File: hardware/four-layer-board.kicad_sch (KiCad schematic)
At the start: 16 parts, among them Q1 AO3401A, U2 AMS1117-3.3

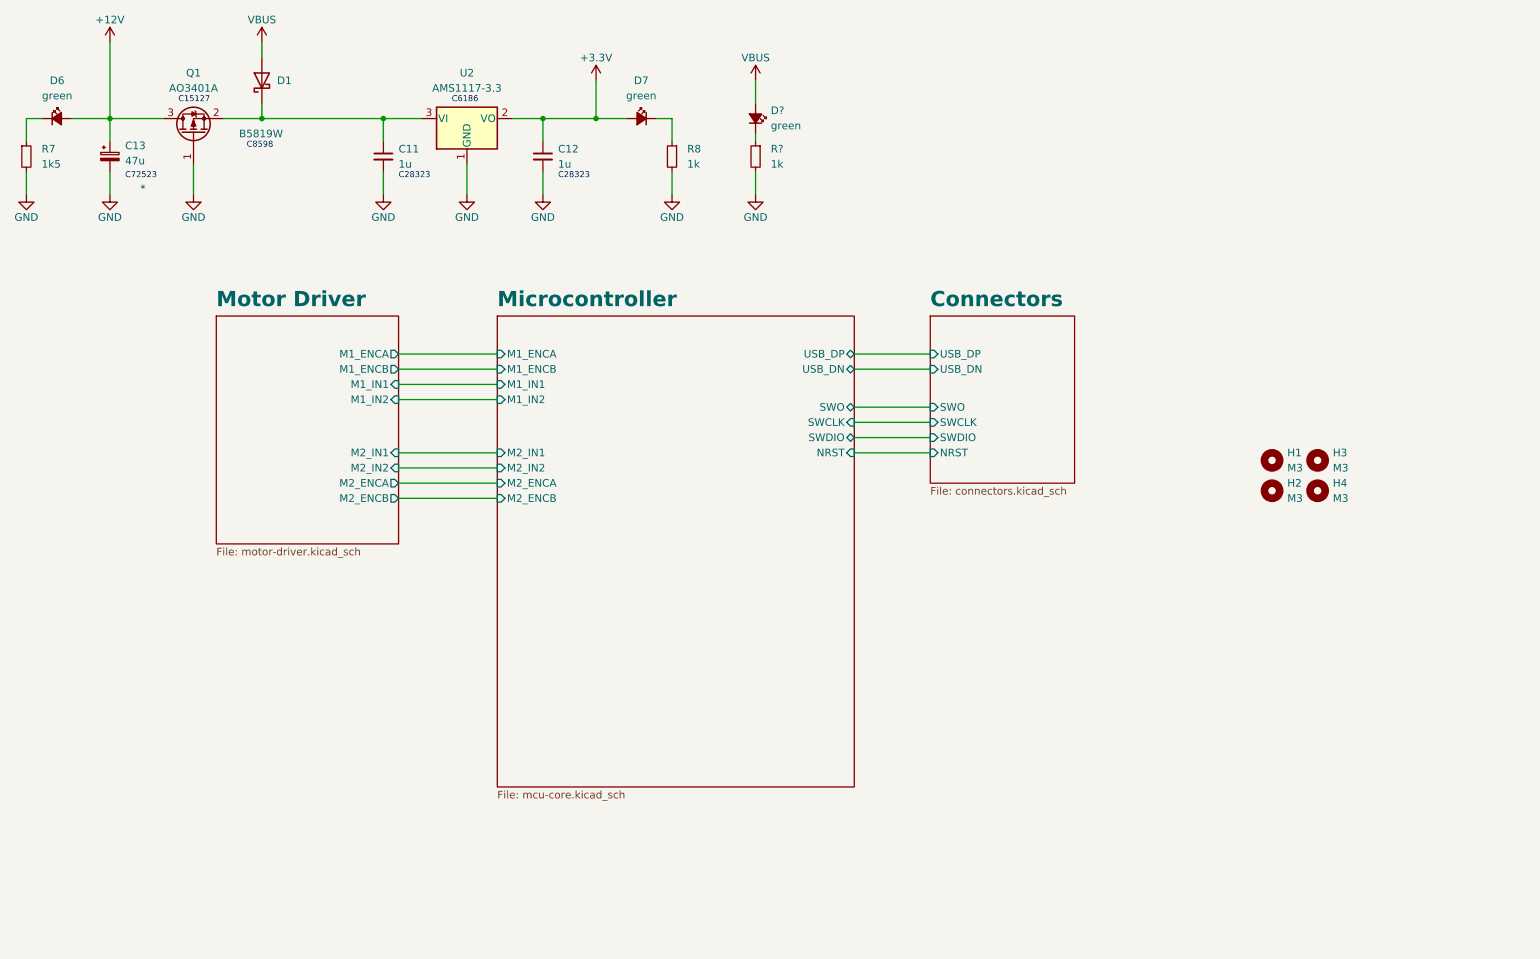
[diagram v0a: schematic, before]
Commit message: Moved hardware to separate directory
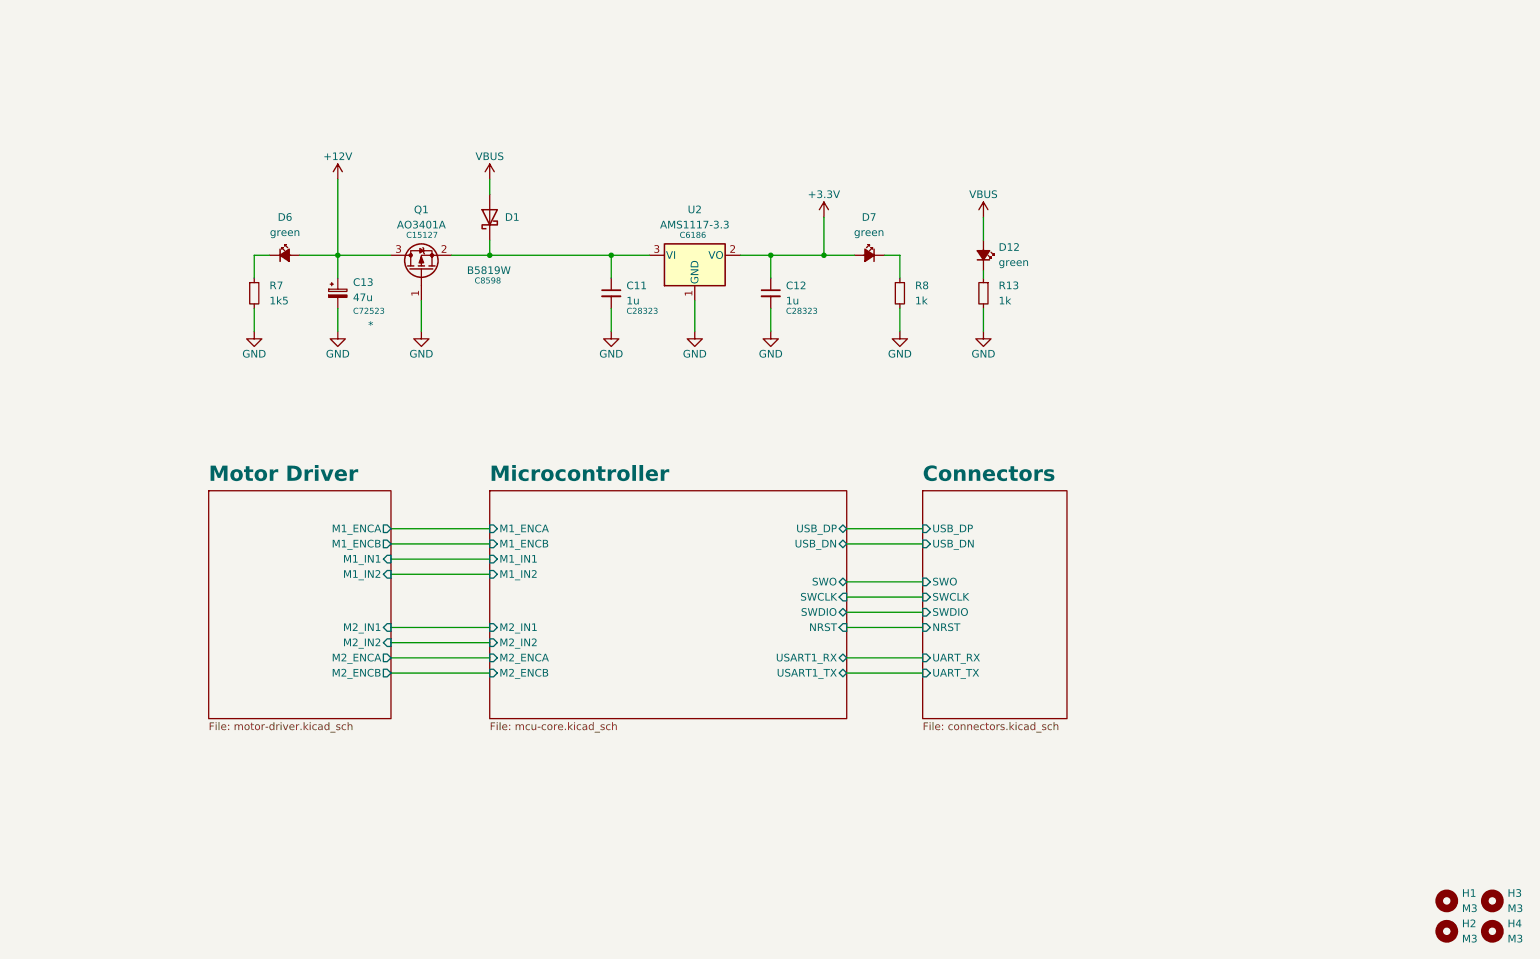
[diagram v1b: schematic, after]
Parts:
- gave numbers to parts that had none: 2
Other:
- sheet Connectors ports: added UART_RX, UART_TX; removed none
- sheet Microcontroller ports: added USART1_RX, USART1_TX; removed none
- company: (none) -> Sampreet SARKAR
- moved on the sheet: C11, C12, C13, D1, D12, D6, D7, H1, H2, H3, H4, Q1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

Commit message: Added pin assignments in firmware
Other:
- title: (none) -> Posit: A STM32 based DC motor controller
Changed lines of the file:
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@@
   (paper "A4")
   (title_block
+    (title "Posit: A STM32 based DC motor controller")
+    (date "2023-06-25")
     (rev "A")
     (company "Sampreet SARKAR")

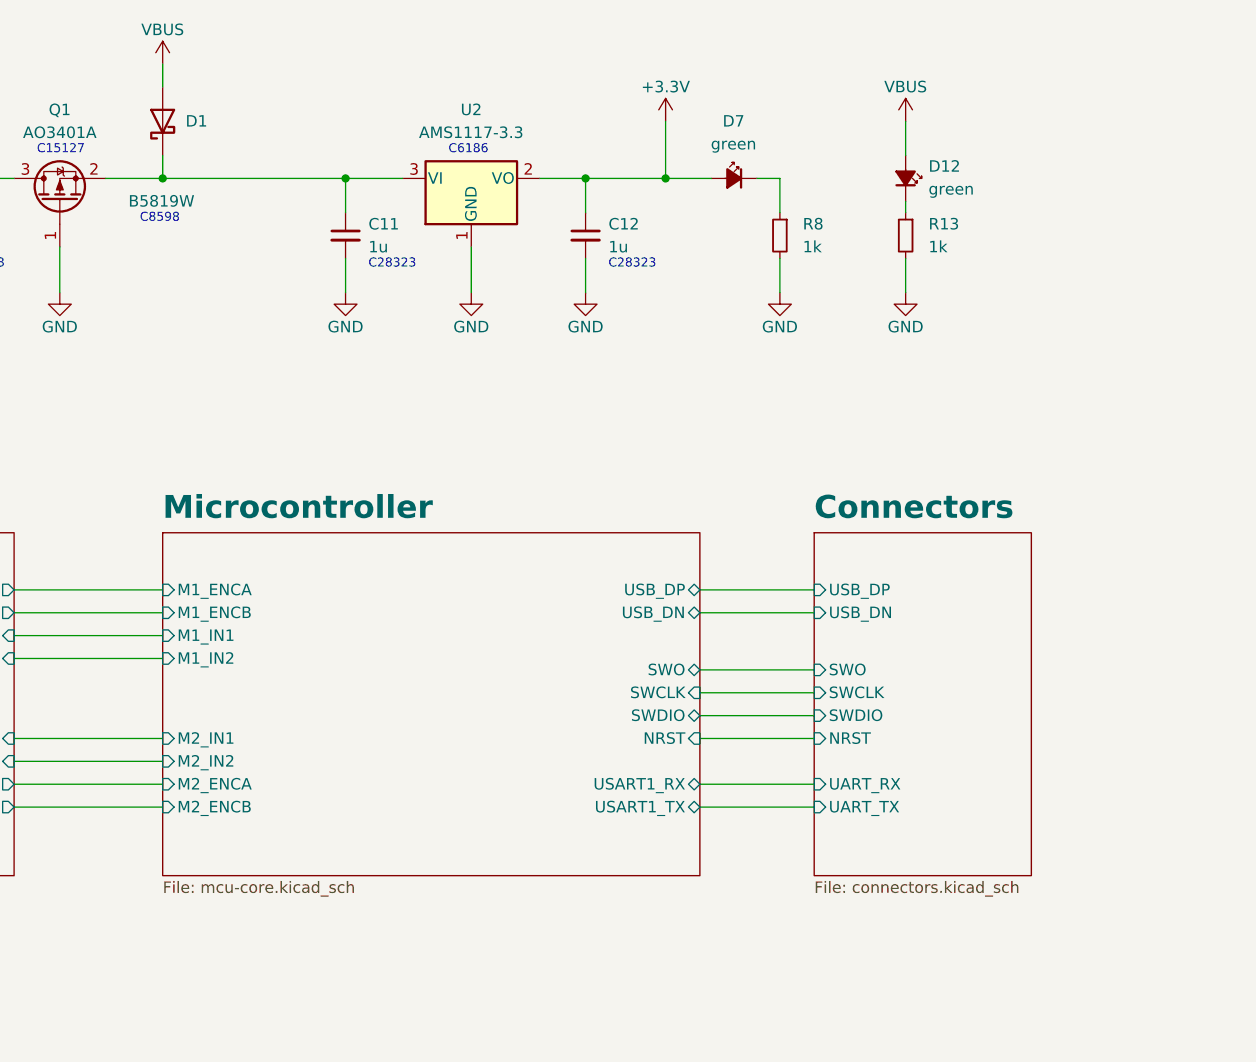
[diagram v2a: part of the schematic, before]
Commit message: Added LEDs and UART
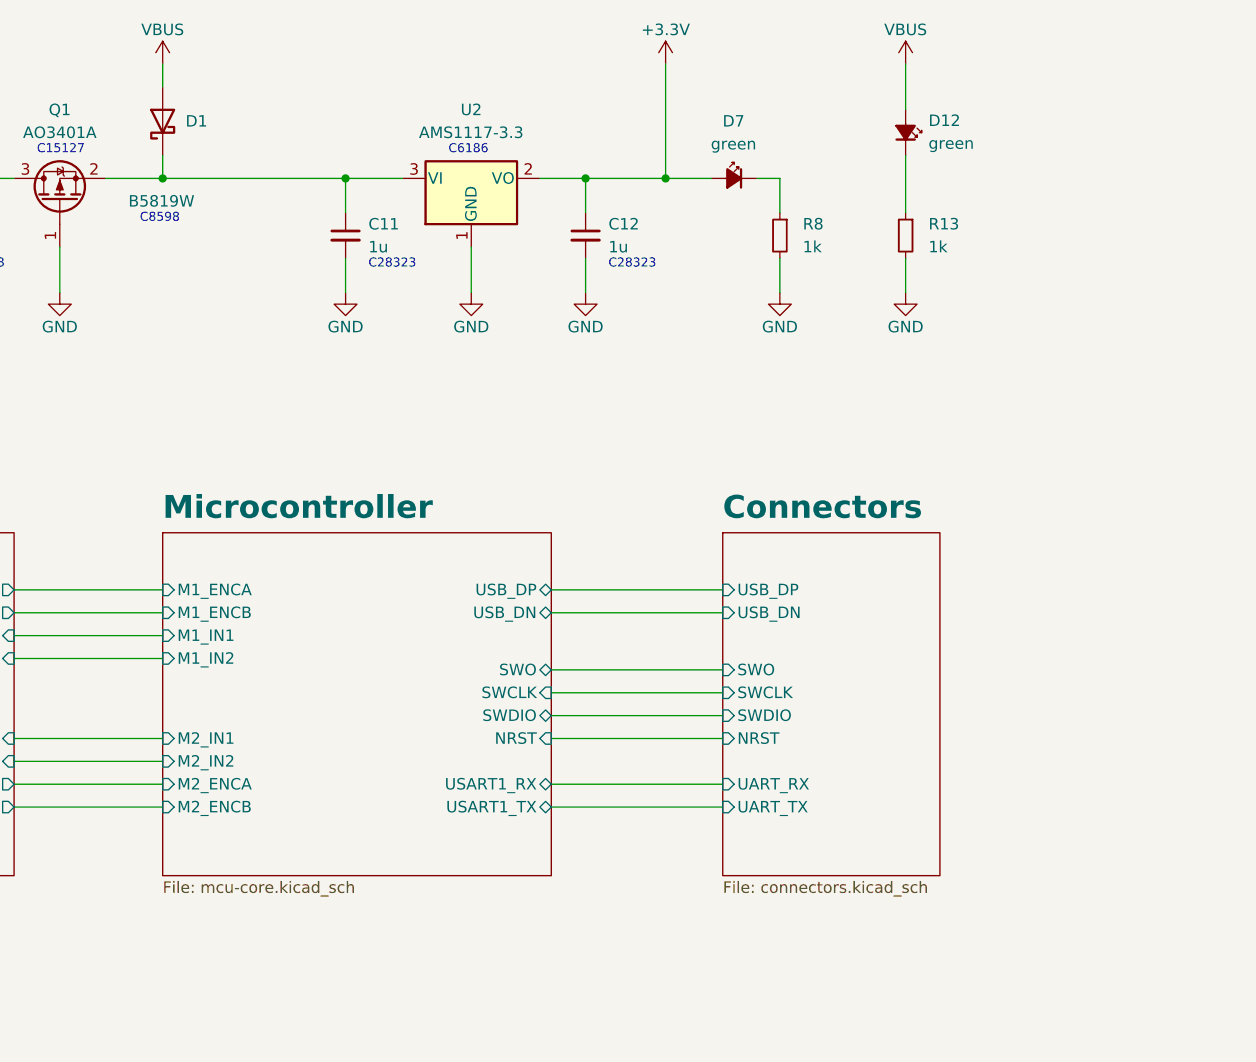
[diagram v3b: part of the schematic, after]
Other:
- moved on the sheet: D12
